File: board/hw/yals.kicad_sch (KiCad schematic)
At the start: 1 part

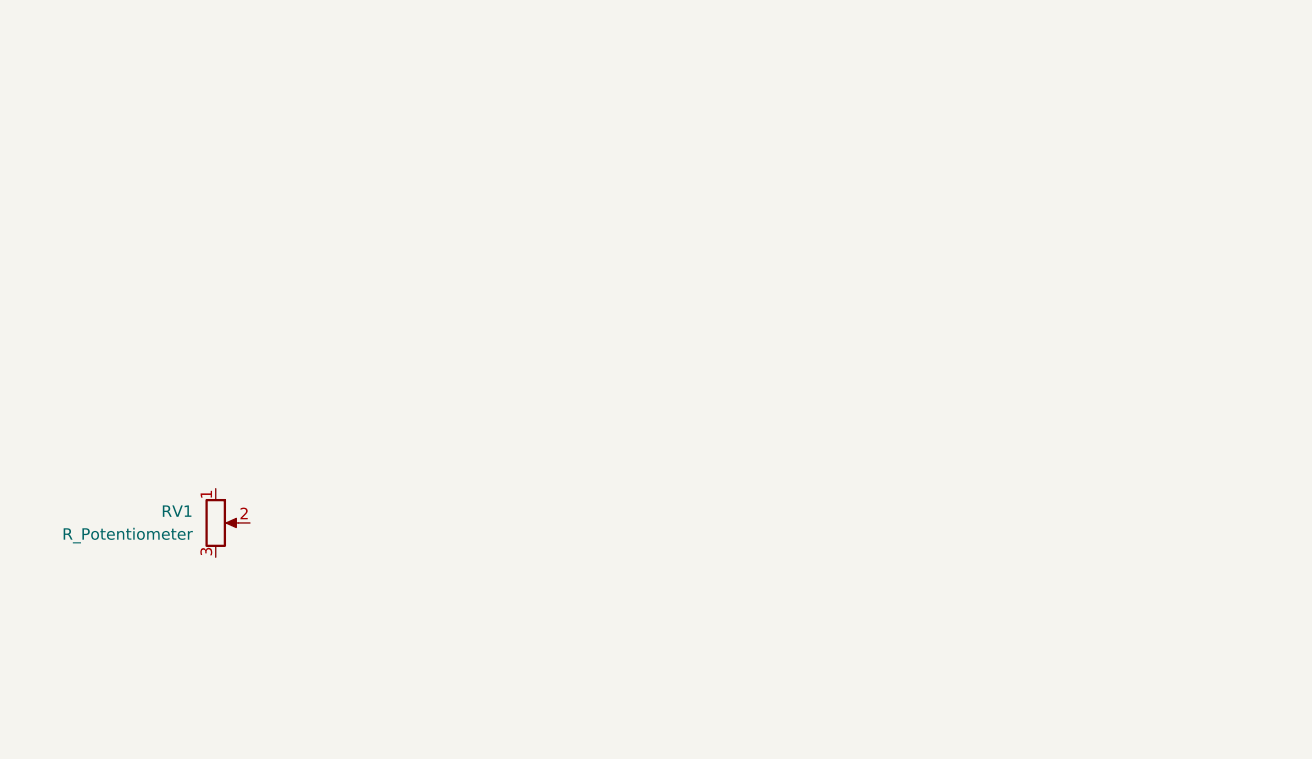
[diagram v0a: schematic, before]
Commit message: added 2 sub-sheets for µC and power
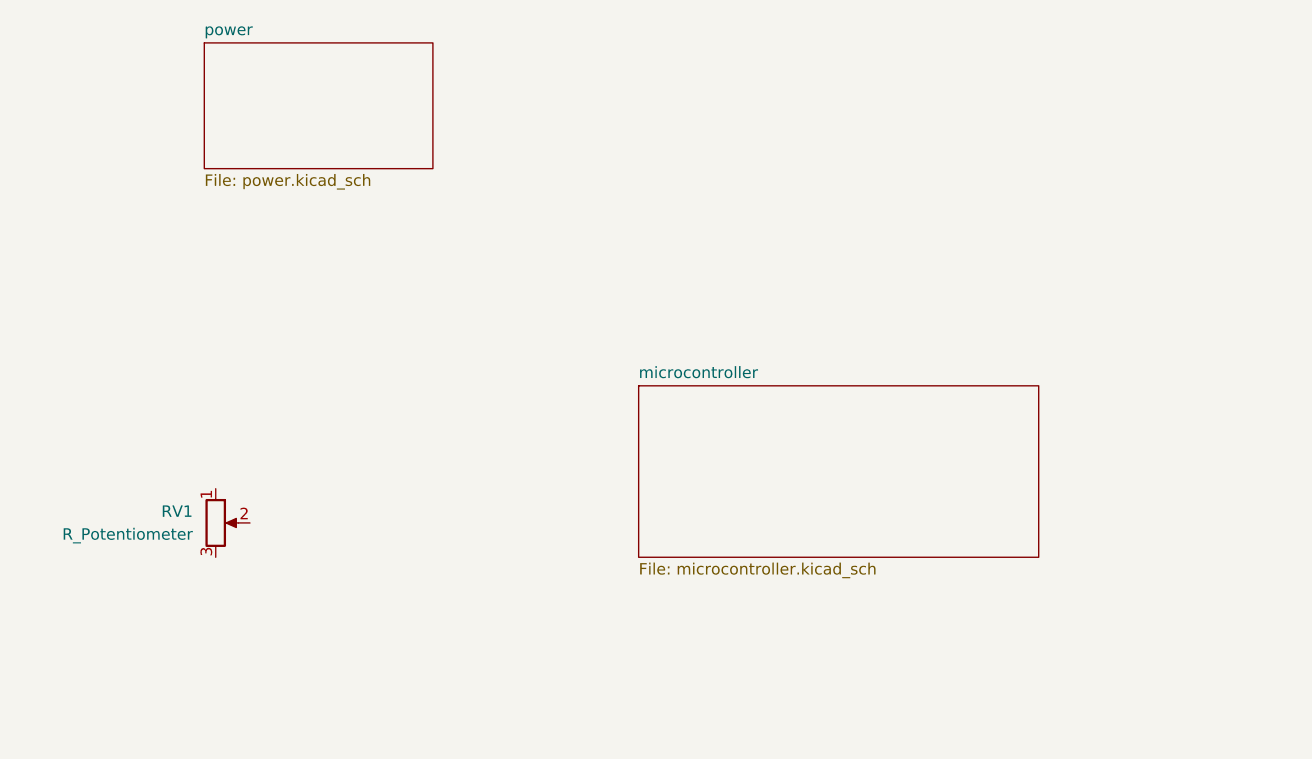
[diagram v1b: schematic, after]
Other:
- added sheet microcontroller (microcontroller.kicad_sch)
- added sheet power (power.kicad_sch)
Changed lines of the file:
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@@
+    )
+  )
+  (sheet (at 73.66 46.99) (size 25.4 13.97) (fields_autoplaced)
+    (stroke (width 0.1524) (type solid))
+    (fill (color 0 0 0 0.0000))
+    (property "Sheetname" "power" (at 73.66 46.2784 0)
+      (effects (font (size 1.27 1.27)) (justify left bottom))
+    )
+    (property "Sheetfile" "power.kicad_sch" (at 73.66 61.5446 0)
+      (effects (font (size 1.27 1.27)) (justify left top))
+    )
+    (instances
+      (project "yals"
+        (path "/920838ab-42d6-4f6a-a4ed-bf4606dd42d5" (page "3"))
+      )
+    )
+  )
+  (sheet (at 121.92 85.09) (size 44.45 19.05) (fields_autoplaced)
+    (stroke (width 0.1524) (type solid))
+    (fill (color 0 0 0 0.0000))
+    (property "Sheetname" "microcontroller" (at 121.92 84.3784 0)
+      (effects (font (size 1.27 1.27)) (justify left bottom))
+    )
+    (property "Sheetfile" "microcontroller.kicad_sch" (at 121.92 104.7246 0)
+      (effects (font (size 1.27 1.27)) (justify left top))
+    )
+    (instances
+      (project "yals"
+        (path "/920838ab-42d6-4f6a-a4ed-bf4606dd42d5" (page "2"))
+      )
     )
   )

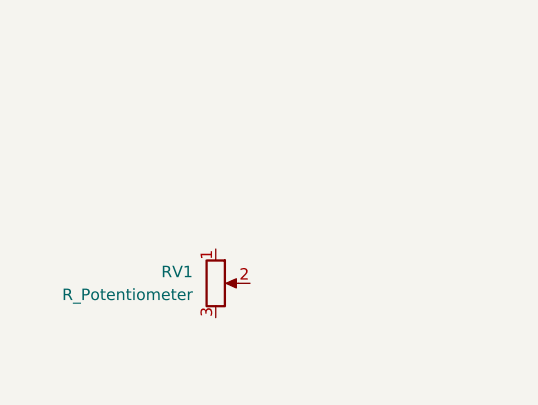
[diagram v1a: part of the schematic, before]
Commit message: added cristal oscillator with capacitors, and 3.3V LDO voltage regulator
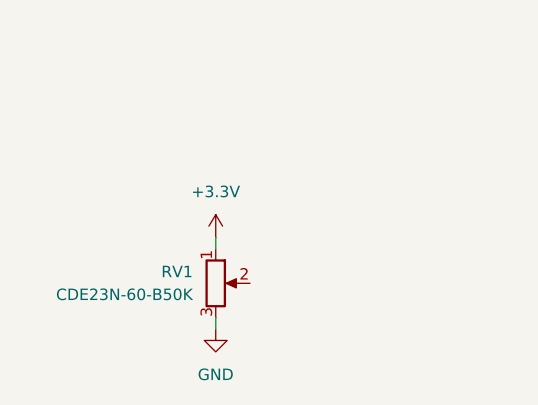
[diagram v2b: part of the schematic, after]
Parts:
- RV1: value R_Potentiometer -> CDE23N-60-B50K
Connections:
- net +3.3V: now reaches RV1.1
- net GND: now reaches RV1.3
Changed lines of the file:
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@@
 (kicad_sch (version 20230121) (generator eeschema)
   (paper "A4")
+  (wire (pts (xy 74.93 95.25) (xy 74.93 96.52))
+    (stroke (width 0) (type default))
+  )
+  (wire (pts (xy 74.93 104.14) (xy 74.93 105.41))
+    (stroke (width 0) (type default))
+  )
   (symbol (lib_id "Device:R_Potentiometer") (at 74.93 100.33 0) (unit 1)
     (in_bom yes) (on_board yes) (dnp no) (fields_autoplaced)
@@
       (effects (font (size 1.27 1.27)) (justify right))
     )
-    (property "Value" "R_Potentiometer" (at 72.39 101.6 0)
+    (property "Value" "CDE23N-60-B50K" (at 72.39 101.6 0)
       (effects (font (size 1.27 1.27)) (justify right))
     )
@@
         )
       )
+    )
+  )
+  (symbol (lib_id "power:GND") (at 74.93 105.41 0) (unit 1)
+    (in_bom yes) (on_board yes) (dnp no) (fields_autoplaced)
+    (property "Reference" "#PWR06" (at 74.93 111.76 0)
+      (effects (font (size 1.27 1.27)) hide)
+    )
+    (property "Value" "GND" (at 74.93 110.49 0)
+      (effects (font (size 1.27 1.27)))
+    )
+    (property "Footprint" "" (at 74.93 105.41 0)
+      (effects (font (size 1.27 1.27)) hide)
+    )
+    (property "Datasheet" "" (at 74.93 105.41 0)
+      (effects (font (size 1.27 1.27)) hide)
+    )
+    (pin "1")
+    (instances
+      (project "yals"
+        (path "/920838ab-42d6-4f6a-a4ed-bf4606dd42d5"
+          (reference "#PWR06") (unit 1)
+        )
+      )
+    )
+  )
+  (symbol (lib_id "power:+3.3V") (at 74.93 95.25 0) (unit 1)
+    (in_bom yes) (on_board yes) (dnp no) (fields_autoplaced)
+    (property "Reference" "#PWR07" (at 74.93 99.06 0)
+      (effects (font (size 1.27 1.27)) hide)
+    )
+    (property "Value" "+3.3V" (at 74.93 90.17 0)
+      (effects (font (size 1.27 1.27)))
+    )
+    (property "Footprint" "" (at 74.93 95.25 0)
+      (effects (font (size 1.27 1.27)) hide)
+    )
+    (property "Datasheet" "" (at 74.93 95.25 0)
+      (effects (font (size 1.27 1.27)) hide)
+    )
+    (pin "1")
+    (instances
+      (project "yals"
+        (path "/920838ab-42d6-4f6a-a4ed-bf4606dd42d5"
+          (reference "#PWR07") (unit 1)
+        )
+      )

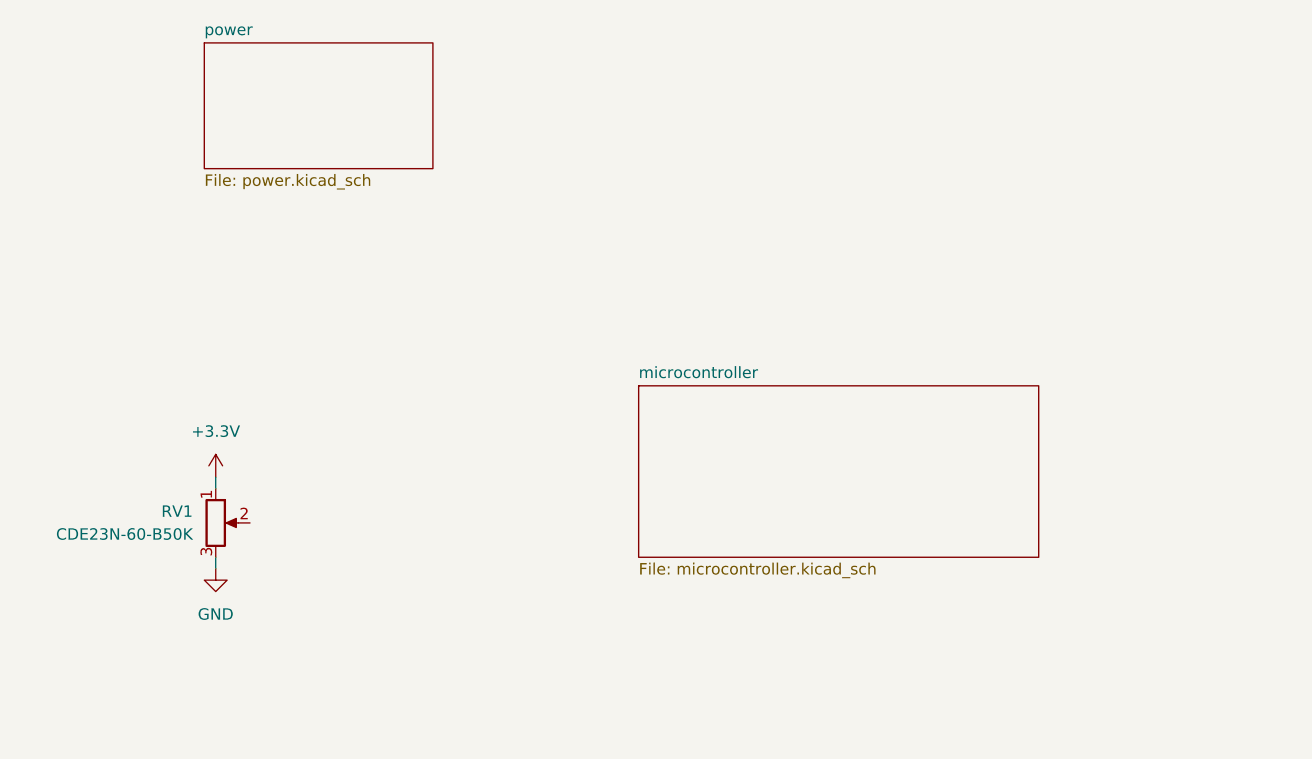
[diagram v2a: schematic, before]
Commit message: rp2040 and its connections are nearly done (still missing power-measuring capabilities)
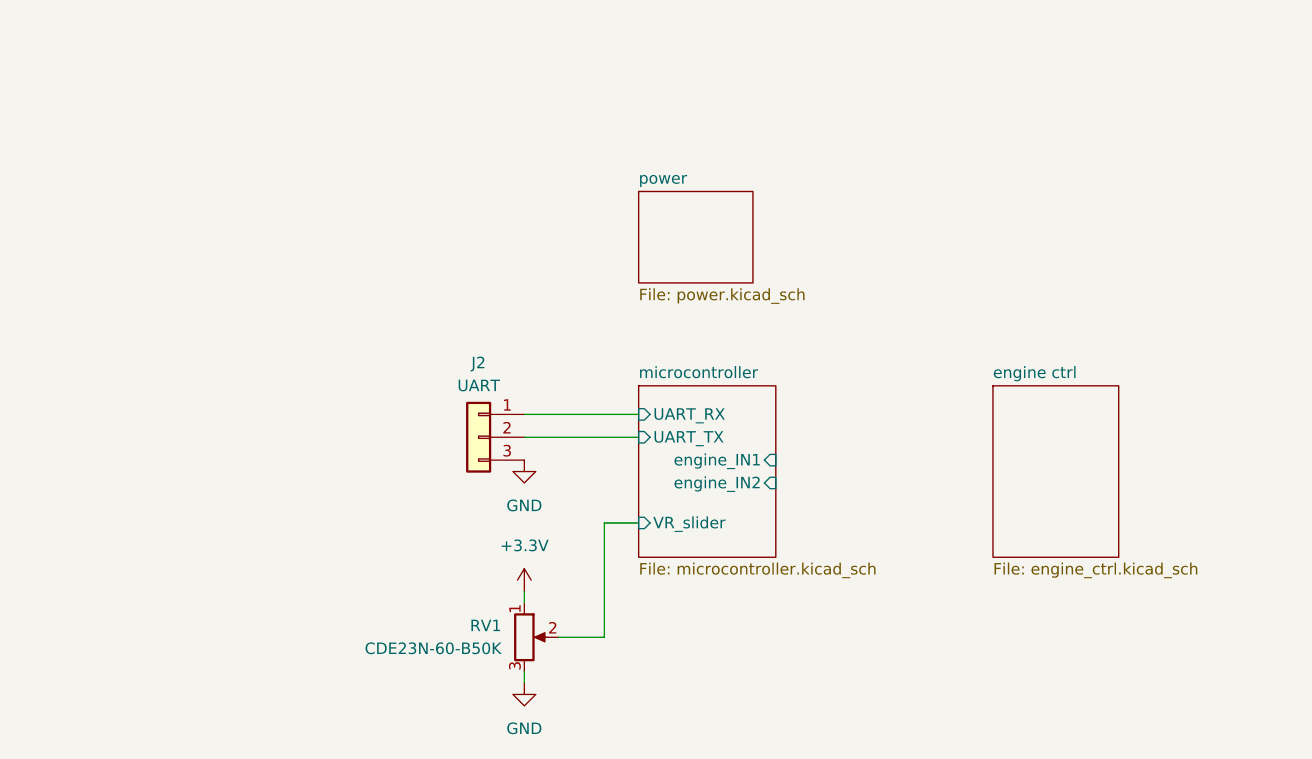
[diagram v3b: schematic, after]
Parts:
- added J2: UART, Connector_PinHeader_2.54mm:PinHeader_1x03_P2.54mm_Vertical, symbol Connector_Generic:Conn_01x03
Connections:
- net GND: now also J2.3 (Pin_3)
- net microcontroller/VR_slider: now reaches RV1.2
- new net microcontroller/UART_RX: J2.1 (Pin_1)
- new net microcontroller/UART_TX: J2.2 (Pin_2)
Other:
- added sheet engine ctrl (engine_ctrl.kicad_sch)
- sheet microcontroller ports: added UART_RX, UART_TX, VR_slider, engine_IN1, engine_IN2; removed none
- moved on the sheet: RV1
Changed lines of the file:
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@@
 (kicad_sch (version 20230121) (generator eeschema)
   (paper "A4")
-  (wire (pts (xy 74.93 95.25) (xy 74.93 96.52))
-    (stroke (width 0) (type default))
-  )
-  (wire (pts (xy 74.93 104.14) (xy 74.93 105.41))
-    (stroke (width 0) (type default))
-  )
-  (symbol (lib_id "Device:R_Potentiometer") (at 74.93 100.33 0) (unit 1)
-    (in_bom yes) (on_board yes) (dnp no) (fields_autoplaced)
-    (property "Reference" "RV1" (at 72.39 99.06 0)
-      (effects (font (size 1.27 1.27)) (justify right))
-    )
-    (property "Value" "CDE23N-60-B50K" (at 72.39 101.6 0)
-      (effects (font (size 1.27 1.27)) (justify right))
-    )
-    (property "Footprint" "st_passives_potentiometers:CDE23N-60-B50K" (at 74.93 100.33 0)
-      (effects (font (size 1.27 1.27)) hide)
-    )
-    (property "Datasheet" "~" (at 74.93 100.33 0)
+  (wire (pts (xy 109.22 107.95) (xy 109.22 109.22))
+    (stroke (width 0) (type default))
+  )
+  (wire (pts (xy 118.11 113.03) (xy 118.11 100.33))
+    (stroke (width 0) (type default))
+  )
+  (wire (pts (xy 109.22 116.84) (xy 109.22 118.11))
+    (stroke (width 0) (type default))
+  )
+  (wire (pts (xy 109.22 90.805) (xy 121.92 90.805))
+    (stroke (width 0) (type default))
+  )
+  (wire (pts (xy 113.03 113.03) (xy 118.11 113.03))
+    (stroke (width 0) (type default))
+  )
+  (wire (pts (xy 109.22 88.265) (xy 121.92 88.265))
+    (stroke (width 0) (type default))
+  )
+  (wire (pts (xy 118.11 100.33) (xy 121.92 100.33))
+    (stroke (width 0) (type default))
+  )
+  (symbol (lib_id "power:GND") (at 109.22 93.345 0) (unit 1)
+    (in_bom yes) (on_board yes) (dnp no) (fields_autoplaced)
+    (property "Reference" "#PWR037" (at 109.22 99.695 0)
+      (effects (font (size 1.27 1.27)) hide)
+    )
+    (property "Value" "GND" (at 109.22 98.425 0)
+      (effects (font (size 1.27 1.27)))
+    )
+    (property "Footprint" "" (at 109.22 93.345 0)
+      (effects (font (size 1.27 1.27)) hide)
+    )
+    (property "Datasheet" "" (at 109.22 93.345 0)
+      (effects (font (size 1.27 1.27)) hide)
+    )
+    (pin "1")
+    (instances
+      (project "yals"
+        (path "/920838ab-42d6-4f6a-a4ed-bf4606dd42d5"
+          (reference "#PWR037") (unit 1)
+        )
+      )
+    )
+  )
+  (symbol (lib_id "Device:R_Potentiometer") (at 109.22 113.03 0) (unit 1)
+    (in_bom yes) (on_board yes) (dnp no) (fields_autoplaced)
+    (property "Reference" "RV1" (at 106.68 111.76 0)
+      (effects (font (size 1.27 1.27)) (justify right))
+    )
+    (property "Value" "CDE23N-60-B50K" (at 106.68 114.3 0)
+      (effects (font (size 1.27 1.27)) (justify right))
+    )
+    (property "Footprint" "st_passives_potentiometers:CDE23N-60-B50K" (at 109.22 113.03 0)
+      (effects (font (size 1.27 1.27)) hide)
+    )
+    (property "Datasheet" "~" (at 109.22 113.03 0)
       (effects (font (size 1.27 1.27)) hide)
     )
@@
     )
   )
-  (symbol (lib_id "power:GND") (at 74.93 105.41 0) (unit 1)
-    (in_bom yes) (on_board yes) (dnp no) (fields_autoplaced)
-    (property "Reference" "#PWR06" (at 74.93 111.76 0)
-      (effects (font (size 1.27 1.27)) hide)
-    )
-    (property "Value" "GND" (at 74.93 110.49 0)
-      (effects (font (size 1.27 1.27)))
-    )
-    (property "Footprint" "" (at 74.93 105.41 0)
-      (effects (font (size 1.27 1.27)) hide)
-    )
-    (property "Datasheet" "" (at 74.93 105.41 0)
+  (symbol (lib_id "power:GND") (at 109.22 118.11 0) (unit 1)
+    (in_bom yes) (on_board yes) (dnp no) (fields_autoplaced)
+    (property "Reference" "#PWR06" (at 109.22 124.46 0)
+      (effects (font (size 1.27 1.27)) hide)
+    )
+    (property "Value" "GND" (at 109.22 123.19 0)
+      (effects (font (size 1.27 1.27)))
+    )
+    (property "Footprint" "" (at 109.22 118.11 0)
+      (effects (font (size 1.27 1.27)) hide)
+    )
+    (property "Datasheet" "" (at 109.22 118.11 0)
       (effects (font (size 1.27 1.27)) hide)
     )
@@
     )
   )
-  (symbol (lib_id "power:+3.3V") (at 74.93 95.25 0) (unit 1)
-    (in_bom yes) (on_board yes) (dnp no) (fields_autoplaced)
-    (property "Reference" "#PWR07" (at 74.93 99.06 0)
-      (effects (font (size 1.27 1.27)) hide)
-    )
-    (property "Value" "+3.3V" (at 74.93 90.17 0)
-      (effects (font (size 1.27 1.27)))
-    )
-    (property "Footprint" "" (at 74.93 95.25 0)
-      (effects (font (size 1.27 1.27)) hide)
-    )
-    (property "Datasheet" "" (at 74.93 95.25 0)
+  (symbol (lib_id "power:+3.3V") (at 109.22 107.95 0) (unit 1)
+    (in_bom yes) (on_board yes) (dnp no) (fields_autoplaced)
+    (property "Reference" "#PWR07" (at 109.22 111.76 0)
+      (effects (font (size 1.27 1.27)) hide)
+    )
+    (property "Value" "+3.3V" (at 109.22 102.87 0)
+      (effects (font (size 1.27 1.27)))
+    )
+    (property "Footprint" "" (at 109.22 107.95 0)
+      (effects (font (size 1.27 1.27)) hide)
+    )
+    (property "Datasheet" "" (at 109.22 107.95 0)
       (effects (font (size 1.27 1.27)) hide)
     )
@@
     )
   )
-  (sheet (at 73.66 46.99) (size 25.4 13.97) (fields_autoplaced)
+  (symbol (lib_id "Connector_Generic:Conn_01x03") (at 104.14 90.805 0) (mirror y) (unit 1)
+    (in_bom yes) (on_board yes) (dnp no) (fields_autoplaced)
+    (property "Reference" "J2" (at 104.14 82.55 0)
+      (effects (font (size 1.27 1.27)))
+    )
+    (property "Value" "UART" (at 104.14 85.09 0)
+      (effects (font (size 1.27 1.27)))
+    )
+    (property "Footprint" "Connector_PinHeader_2.54mm:PinHeader_1x03_P2.54mm_Vertical" (at 104.14 90.805 0)
+      (effects (font (size 1.27 1.27)) hide)
+    )
+    (property "Datasheet" "~" (at 104.14 90.805 0)
+      (effects (font (size 1.27 1.27)) hide)
+    )
+    (pin "2")
+    (pin "1")
+    (pin "3")
+    (instances
+      (project "yals"
+        (path "/920838ab-42d6-4f6a-a4ed-bf4606dd42d5"
+          (reference "J2") (unit 1)
+        )
+      )
+    )
+  )
+  (sheet (at 121.92 63.5) (size 12.7 10.16) (fields_autoplaced)
     (stroke (width 0.1524) (type solid))
     (fill (color 0 0 0 0.0000))
-    (property "Sheetname" "power" (at 73.66 46.2784 0)
+    (property "Sheetname" "power" (at 121.92 62.7884 0)
       (effects (font (size 1.27 1.27)) (justify left bottom))
     )
-    (property "Sheetfile" "power.kicad_sch" (at 73.66 61.5446 0)
+    (property "Sheetfile" "power.kicad_sch" (at 121.92 74.2446 0)
       (effects (font (size 1.27 1.27)) (justify left top))
     )
@@
     )
   )
-  (sheet (at 121.92 85.09) (size 44.45 19.05) (fields_autoplaced)
+  (sheet (at 121.92 85.09) (size 15.24 19.05) (fields_autoplaced)
     (stroke (width 0.1524) (type solid))
     (fill (color 0 0 0 0.0000))
@@
       (effects (font (size 1.27 1.27)) (justify left top))
     )
+    (pin "VR_slider" input (at 121.92 100.33 180)
+      (effects (font (size 1.27 1.27)) (justify left))
+    )
+    (pin "UART_RX" input (at 121.92 88.265 180)
+      (effects (font (size 1.27 1.27)) (justify left))
+    )
+    (pin "UART_TX" input (at 121.92 90.805 180)
+      (effects (font (size 1.27 1.27)) (justify left))
+    )
+    (pin "engine_IN1" input (at 137.16 93.345 0)
+      (effects (font (size 1.27 1.27)) (justify right))
+    )
+    (pin "engine_IN2" input (at 137.16 95.885 0)
+      (effects (font (size 1.27 1.27)) (justify right))
+    )
     (instances
       (project "yals"
@@
       )
     )
+  )
+  (sheet (at 161.29 85.09) (size 13.97 19.05) (fields_autoplaced)
+    (stroke (width 0.1524) (type solid))
+    (fill (color 0 0 0 0.0000))
+    (property "Sheetname" "engine ctrl" (at 161.29 84.3784 0)
+      (effects (font (size 1.27 1.27)) (justify left bottom))
+    )
+    (property "Sheetfile" "engine_ctrl.kicad_sch" (at 161.29 104.7246 0)
+      (effects (font (size 1.27 1.27)) (justify left top))
+    )
+    (instances
+      (project "yals"
+        (path "/920838ab-42d6-4f6a-a4ed-bf4606dd42d5" (page "4"))
+      )
+    )
